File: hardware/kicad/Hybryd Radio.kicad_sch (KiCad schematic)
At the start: 80 parts, among them J1 12V IN, J10 EC11, J11 BTN PWR, J2 5V to P4 USB-C, J3 to P4 J3, J4 ANT, J5 SPK L, J6 SPK R, J7 PRESETS+MODE, J8 SPARE, J9 EC11, Q1 IRF4905, U1 WeAct-SY8205, U2 HT7333-A, U3 RRD-102, U4 GY-PCM5102A, U5 MCP23017-CJMCU

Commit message: Плата-носитель: исправлены ошибки, найденные самопроверкой
Схема:
- Разделительные 4,7 мкФ на выходах LOUT/ROUT тюнера. У RDA5807M
  выходы сидят на постоянном напряжении 1,0-1,1 В (даташит V1.1, с. 7),
  в типовой схеме производителя (рис. 8-1) стоят 4,7 мкФ. Без них
  постоянка шла в узел микшера и через 10 кОм в выход ЦАП. Ошибка
  тянулась со сборки на Pi.
- Последовательный 100 пФ на входе антенны — как C7 в той же схеме.
- Линия отключения усилителей: места под 100 кОм вниз (вывод SDZ, LOW
  выключает) и вверх на +3V3_ESP (вывод MUTE, HIGH выключает) — у TPA3118
  оба есть с обратной логикой (даташит TI, с. 4), а куда идёт площадка
  MUTE на HW-327, неизвестно. Впаивается один резистор по прозвонке.

Документы:
- «Перемычки GAIN» нет: усиление задаёт делитель на выводе 8 (с. 14).
- Уровень тюнера 360 мВ в даташите есть (с. 7) — исправлено в docs/04,
  docs/26, docs/33.
- 5,1 В -> 5,0 В (модуль WeAct SY8205).
- 47 Ом в I2S не защищают ЦАП — довод снят.
- Для прерываний расширителя нужен IOCON.MIRROR = 1 (MCP23017, с. 20).
Полный список — docs/33, §11. Схема пересобрана: 66 цепей, расхождений 0.

Co-Authored-By: Claude Opus 5.5 <noreply@anthropic.com>
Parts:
- removed C10: 100n, Capacitor_THT:C_Disc_D5.0mm_W2.5mm_P5.00mm, symbol Device:C
- removed C11, C16: 3u3 film 63V, Capacitor_THT:C_Rect_L18.0mm_W8.0mm_P15.00mm_FKS3_FKP3, symbol Device:C
- removed C13, C17: 1000u 25V, Capacitor_THT:CP_Radial_D12.5mm_P5.00mm, symbol Device:C_Polarized
- removed C20: 10n, Capacitor_THT:C_Disc_D5.0mm_W2.5mm_P5.00mm, symbol Device:C
- added C10, C11: 4u7 25V, Capacitor_THT:CP_Radial_D5.0mm_P2.00mm, symbol Device:C_Polarized
- added C13, C17: 100n, Capacitor_THT:C_Disc_D5.0mm_W2.5mm_P5.00mm, symbol Device:C
- added C16, C20: 1000u 25V, Capacitor_THT:CP_Radial_D12.5mm_P5.00mm, symbol Device:C_Polarized
- added C24, C25, C26: 10n, Capacitor_THT:C_Disc_D5.0mm_W2.5mm_P5.00mm, symbol Device:C
- added R21: 1k, Resistor_THT:R_Axial_DIN0207_L6.3mm_D2.5mm_P10.16mm_Horizontal, symbol Device:R
- C12: value 3u3 film 63V -> 100p C0G; footprint Capacitor_THT:C_Rect_L18.0mm_W8.0mm_P15.00mm_FKS3_FKP3 -> Capacitor_THT:C_Disc_D5.0mm_W2.5mm_P5.00mm
- C14, C18, C19: value 100n -> 3u3 film 63V; footprint Capacitor_THT:C_Disc_D5.0mm_W2.5mm_P5.00mm -> Capacitor_THT:C_Rect_L18.0mm_W8.0mm_P15.00mm_FKS3_FKP3
- C21, C22: value 10n -> 100n
- R14: value 100k -> 100k (SDZ)
- R15: value 10k -> 100k (MUTE)
- R19: value 2k2 -> 10k
- R20: value 1k -> 2k2
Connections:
- net +12V: now also C21.1, R20.1, C16.1, C17.1, C20.1; no longer C14.1, C18.1, R19.1
- net +3V3_ESP: now also C22.1, R19.2; no longer C19.1
- net +5V: now also C13.1, R21.1; no longer R20.1
- net AMP_L_INN: now also C15.1; no longer C12.1
- net AMP_L_INP: now also C14.2
- net AMP_R_INN: now also C19.1
- net AMP_R_INP: now also C18.2; no longer C15.2
- net AMP_SD: now also R15.1
- net ANT: now also C12.2; no longer J4.1 (Pin_1)
- net ENC1_A: now also C23.1, R16.1; no longer R15.1
- net ENC1_B: now also R17.1, C24.1; no longer C21.1, R16.1
- net ENC2_A: now also R18.1, C25.1; no longer C22.1, R17.1
- net ENC2_B: now also R19.1, C26.1; no longer C23.1, R18.1
- net GND: now also C15.2, C13.2, C16.2, C17.2, C20.2, C24.2, C25.2, C26.2; no longer C12.2, C14.2, C18.2
- net LED_12V: now also R20.2; no longer R19.2
- net LED_5V: now also R21.2; no longer R20.2
- net MIX_L: now also C14.1
- net MIX_R: now also C18.1; no longer C15.1
- net TUNER_L: now also C10.2; no longer U3.7 (LOUT)
- net TUNER_R: now also C11.2; no longer U3.8 (ROUT)
- new net ANT_IN: C12.1, J4.1 (Pin_1)
- new net RDA_LOUT: C10.1, U3.7 (LOUT)
- new net RDA_ROUT: C11.1, U3.8 (ROUT)
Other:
- note added: "C на LOUT/ROUT обязательны: у RDA5807M на выходах ~1,05 В постоянки"
- note added: "Впаять ОДИН из двух 100k: (SDZ) на GND или (MUTE) на +3V3 —"
- note added: "по прозвонке площадки MUTE HW-327: вывод 2 SDZ или 12 MUTE TPA3118"
- note removed: "R14 подобрать по замеру MUTE модуля HW-327 (docs/33, §8)"

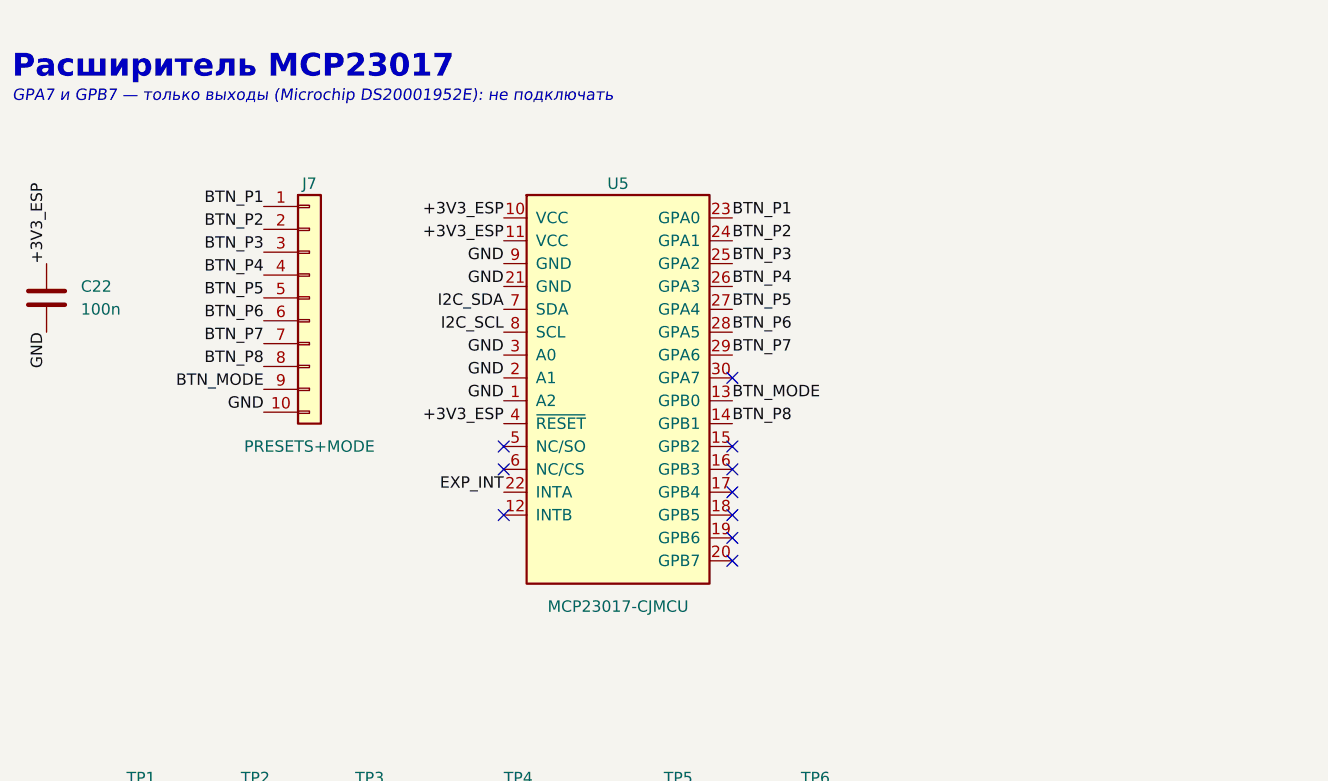
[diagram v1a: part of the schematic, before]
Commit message: Плата-носитель: посадочные места модулей, пайка проводов органов управления
Посадочные места всех пяти модулей (hardware/skidl/make_footprints.py ->
hybrid-radio.pretty), геометрия и источники — docs/33, §13:
- RRD-102: площадки по библиотеке JLCEDA (LCSC C9900205627); раскладка
  совпала с реверсом модуля (briankhuu.com, 2015) — паять микросхемой вверх.
- GY-PCM5102A, MCP23017-CJMCU: в гнёзда 2,54, микросхемой вверх (подтверждено).
  Взаимное положение рядов ЦАП — по центрам отверстий на фото, сходится с
  замером до 0,05 мм (первая оценка была неточной на 0,3 мм — исправлено).
  MCP23017: одиночный ряд в 7 шагах от столбца A — 8 шагов не влезают.
- WeAct SY8205, HW-327: на стойках, выводы проводами 0,5 мм² — у модулей
  площадки под провод, а не под штыри. Отверстия по замерам заказчика.
Номера площадок сверяются с выводами символов (проверка в скрипте,
на поломке проверена). ERC KiCad — 0 нарушений.

Энкодеры, кнопка питания, пресеты и MODE — провода паяются в плату вместо
JST XH (решение заказчика): Connector_Wire 0,25 мм². Пресеты разбиты на
J7 (1-4) и J12 (5-8, MODE): серия в KiCad не длиннее 6 контактов.

.gitignore: .history/ — локальная история KiCad 10 со своим git.

Открыто: крепёж модулей — отверстия под стойки 3,2 мм пока заглушка;
проверка всех посадочных мест печатью 1:1 до заказа плат.

Co-Authored-By: Claude Opus 5.5 <noreply@anthropic.com>
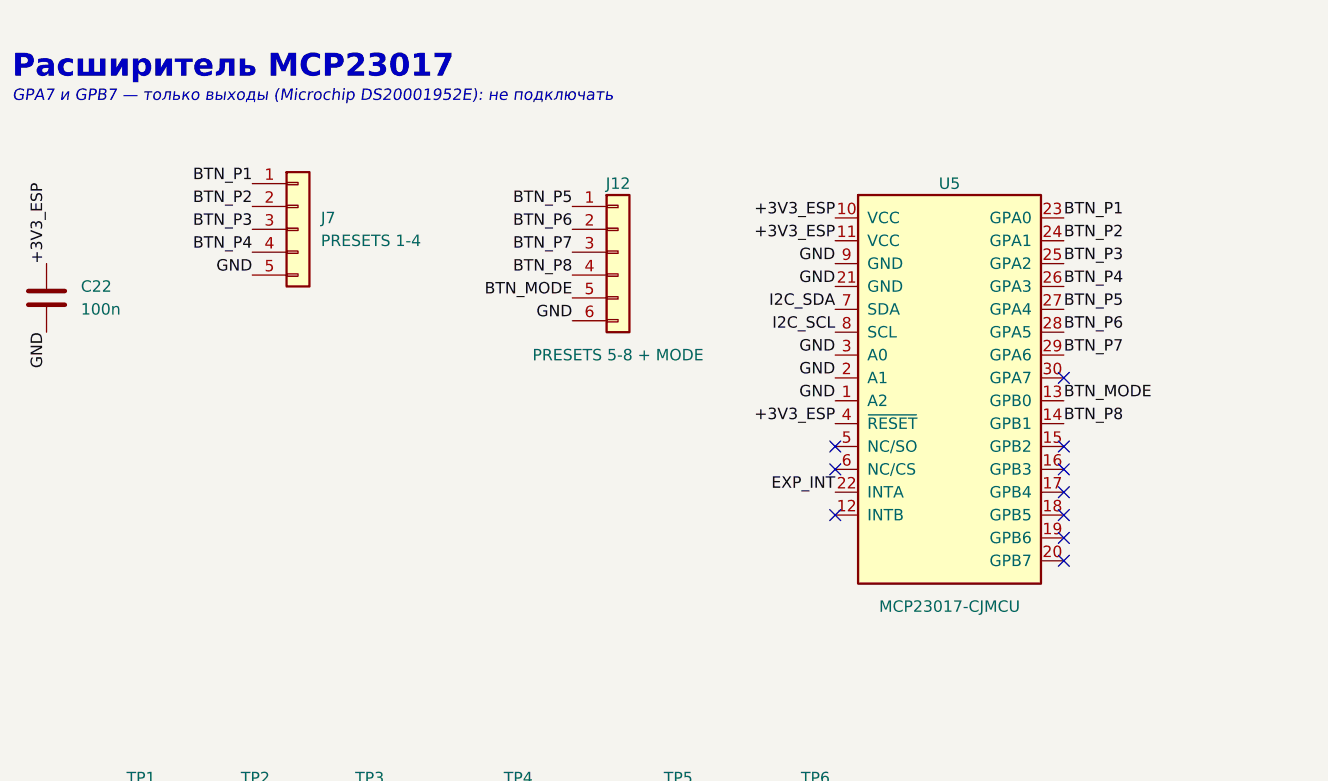
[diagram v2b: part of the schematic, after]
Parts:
- removed J7: PRESETS+MODE, Connector_JST:JST_XH_B10B-XH-A_1x10_P2.50mm_Vertical, symbol Connector_Generic:Conn_01x10
- added J12: PRESETS 5-8 + MODE, Connector_Wire:SolderWire-0.25sqmm_1x06_P4.2mm_D0.65mm_OD1.7mm, symbol Connector_Generic:Conn_01x06
- added J7: PRESETS 1-4, Connector_Wire:SolderWire-0.25sqmm_1x05_P4.2mm_D0.65mm_OD1.7mm, symbol Connector_Generic:Conn_01x05
- J10, J9: footprint Connector_JST:JST_XH_B5B-XH-A_1x05_P2.50mm_Vertical -> Connector_Wire:SolderWire-0.25sqmm_1x05_P4.2mm_D0.65mm_OD1.7mm
- J11: footprint Connector_JST:JST_XH_B2B-XH-A_1x02_P2.50mm_Vertical -> Connector_Wire:SolderWire-0.25sqmm_1x02_P4.2mm_D0.65mm_OD1.7mm
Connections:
- net BTN_MODE: now also J12.5 (Pin_5)
- net BTN_P1: now also J7.1 (Pin_1)
- net BTN_P2: now also J7.2 (Pin_2)
- net BTN_P3: now also J7.3 (Pin_3)
- net BTN_P4: now also J7.4 (Pin_4)
- net BTN_P5: now also J12.1 (Pin_1)
- net BTN_P6: now also J12.2 (Pin_2)
- net BTN_P7: now also J12.3 (Pin_3)
- net BTN_P8: now also J12.4 (Pin_4)
- net GND: now also J12.6 (Pin_6), J7.5 (Pin_5)

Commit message: Доп. платы к P4, кнопки пресетов на MCP23017, Raspberry Pi помечен неактуальным
Прошивка:
- драйвер расширителя MCP23017 в модуле ввода: опрос портов по I2C
  в цикле ввода (5 мс), подтяжки, GPA7/GPB7 - выходы с нулём (только
  выходы, Microchip DS20001952D); пресеты 1-7 GPA0-6, пресет 8 GPB0,
  MODE GPB1 - по фактической проводке макета;
- защита от ложных нажатий: проверка настройки расширителя раз в
  секунду с повторной настройкой и отбраковка чтений, где нажато
  больше двух кнопок. Ложные удержания перезаписали ячейки пресетов
  (2026-10-19), причина не установлена - журнал того момента не снят;
- одноразовые ключи записи станций в банки (выключены после записи),
  отладочный вывод ввода IPRADIO_DEBUG_INPUT пока включён.
Проверено на плате: все 8 пресетов интернет-радио переключаются.

Железо (hardware/skidl, hardware/kicad):
- три платы: питание (разведена, односторонняя), сигнальная
  (расставлена заново после правки RRD-102, НЕ разведена - по просьбе
  заказчика), площадка усилителей (расставлена);
- сверка с руководством разводки: развязка у выводов, срез углов 45,
  сшивка земли, солид у силовых площадок, шелкография, надписи;
- RRD-102: выводы 3 и 9 - NC (прозвонено на модуле, в библиотеке
  JLCEDA были GND); C27 100 нФ у питания тюнера;
- лист для макетирования hardware/kicad/carriers: один лист A1, все
  соединения проводами (sch_router.py), ERC 0, нетлист совпадает.
Расхождение: в схеме пресет 8 на GPB1, MODE на GPB0 - на макете
наоборот, схему ещё привести к проводке.

Документы:
- docs/35: состав доп. плат и перечень 91 детали;
- документы ревизии на Raspberry Pi помечены «НЕАКТУАЛЬНО», в
  остальных упоминания исправлены; README под сборку на ESP32-P4;
- docs/33 §15-16: сверка с руководством разводки, отказ от модулей
  AC-DC; перемычки H1L-H4L модуля PCM5102A прозвонены.

Co-Authored-By: Claude Opus 5.5 <noreply@anthropic.com>
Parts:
- removed J1: 12V IN, TerminalBlock_Phoenix:TerminalBlock_Phoenix_MKDS-1,5-2-5.08_1x02_P5.08mm_Horizontal, symbol Connector:Screw_Terminal_01x02
- added C27: 100n, Capacitor_THT:C_Disc_D5.0mm_W2.5mm_P5.00mm, symbol Device:C
- added J1: 12V 5.5x2.1, Connector_BarrelJack:BarrelJack_Horizontal, symbol Connector:Barrel_Jack_Switch
- added J13: 12V to AMP, TerminalBlock_Phoenix:TerminalBlock_Phoenix_MKDS-1,5-2-5.08_1x02_P5.08mm_Horizontal, symbol Connector:Screw_Terminal_01x02
- added J14: 5V to SIGNAL, TerminalBlock_Phoenix:TerminalBlock_Phoenix_MKDS-1,5-3-5.08_1x03_P5.08mm_Horizontal, symbol Connector:Screw_Terminal_01x03
- added J15: 5V IN, TerminalBlock_Phoenix:TerminalBlock_Phoenix_MKDS-1,5-3-5.08_1x03_P5.08mm_Horizontal, symbol Connector:Screw_Terminal_01x03
- added J16: TO AMPS, Connector_Wire:SolderWire-0.25sqmm_1x06_P4.2mm_D0.65mm_OD1.7mm, symbol Connector_Generic:Conn_01x06
- added J17: 12V IN, TerminalBlock_Phoenix:TerminalBlock_Phoenix_MKDS-1,5-2-5.08_1x02_P5.08mm_Horizontal, symbol Connector:Screw_Terminal_01x02
- J10, J11, J12, J7, J9, TP1, TP2, TP8: now left out of the parts list
- TP3: value +3V3_FM -> GND; now left out of the parts list
- TP4: value PWR_SENSE -> +3V3_FM; now left out of the parts list
- TP5: value SUM_L -> PWR_SENSE; now left out of the parts list
- TP6: value SUM_R -> SUM_L; now left out of the parts list
- TP7: value GND -> SUM_R; now left out of the parts list
- U2: footprint Package_TO_SOT_THT:TO-92_Inline -> Package_TO_SOT_THT:TO-92_Inline_Wide
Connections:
- net +12V: now also J13.1 (Pin_1), J17.1 (Pin_1)
- net +12V_IN: now also J1.1
- net +3V3_FM: now also TP4.1, C27.1; no longer TP3.1
- net +5V: now also J14.1 (Pin_1), J15.1 (Pin_1)
- net AMP_L_INN: now also J16.2 (Pin_2)
- net AMP_L_INP: now also J16.1 (Pin_1)
- net AMP_R_INN: now also J16.4 (Pin_4)
- net AMP_R_INP: now also J16.3 (Pin_3)
- net AMP_SD: now also J16.5 (Pin_5)
- net GND: now also TP3.1, C27.2, J1.2, J13.2 (Pin_2), J14.2 (Pin_2), J15.2 (Pin_2), J16.6 (Pin_6), J17.2 (Pin_2); no longer TP7.1, U3.3 (GND), U3.9 (GND)
- net PWR_SENSE: now also TP5.1, J14.3 (Pin_3), J15.3 (Pin_3); no longer TP4.1
- net SUM_L: now also TP6.1; no longer TP5.1
- net SUM_R: now also TP7.1; no longer TP6.1
- no-connect marks 25 -> 28
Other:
- note added: "Индикация и контрольные точки питания"
- note added: "Контрольные точки"
- note added: "Разъём: 12 В с платы питания"
- note added: "Разъёмы: 12 В на усилители, 5 В на сигнальную плату"
- note added: "Разъёмы: питание, провода к усилителям"
- note removed: "Индикация и контрольные точки"
- title: IP-Radio: плата-носитель модулей -> Разъём: 12 В с платы питания
